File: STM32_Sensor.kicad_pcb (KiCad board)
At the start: 2 copper layers, 35.6 x 20.3 mm, 27 parts, among them J1 Conn Side, J2 Conn Down, J3 Conn Up, J4 Conn Prog, J5 u.FL, SW1 SW_Reset, SW2 SW_BOOT, U1 STM32F103C8Tx, U2 RFM69CW, U3 RFM69HW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

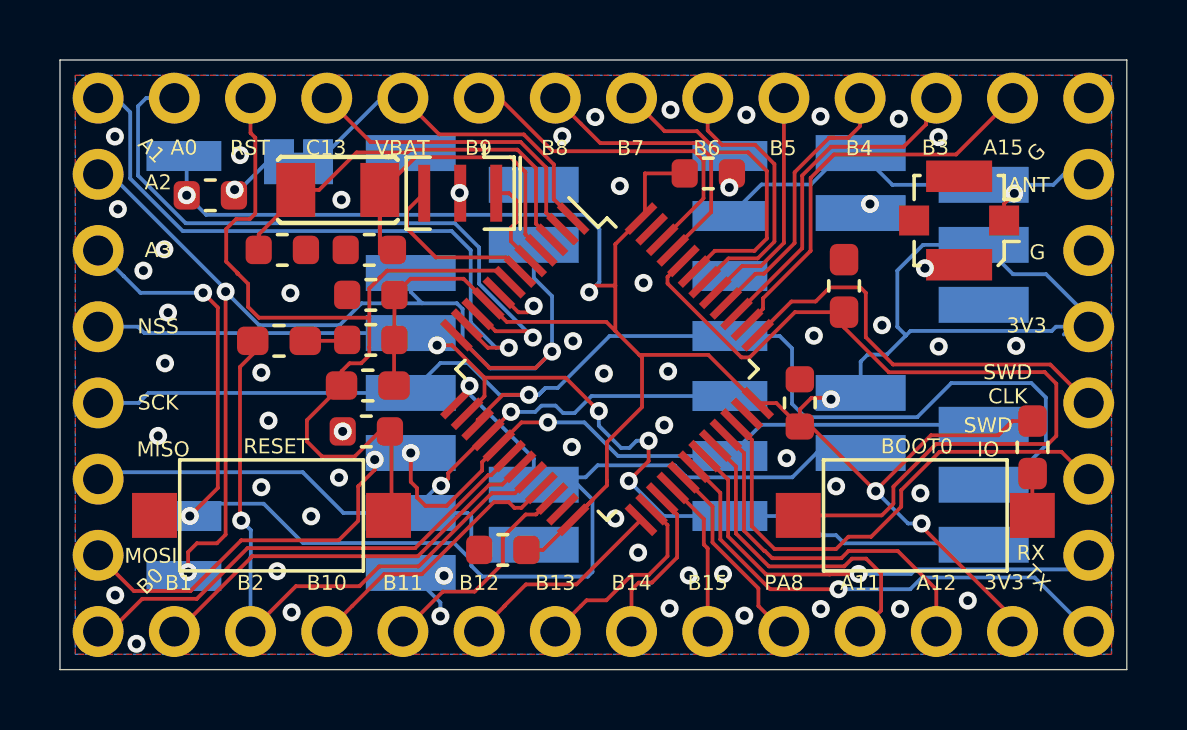
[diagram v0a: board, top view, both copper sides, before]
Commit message: Routed the board with 6 mils traces/clearance
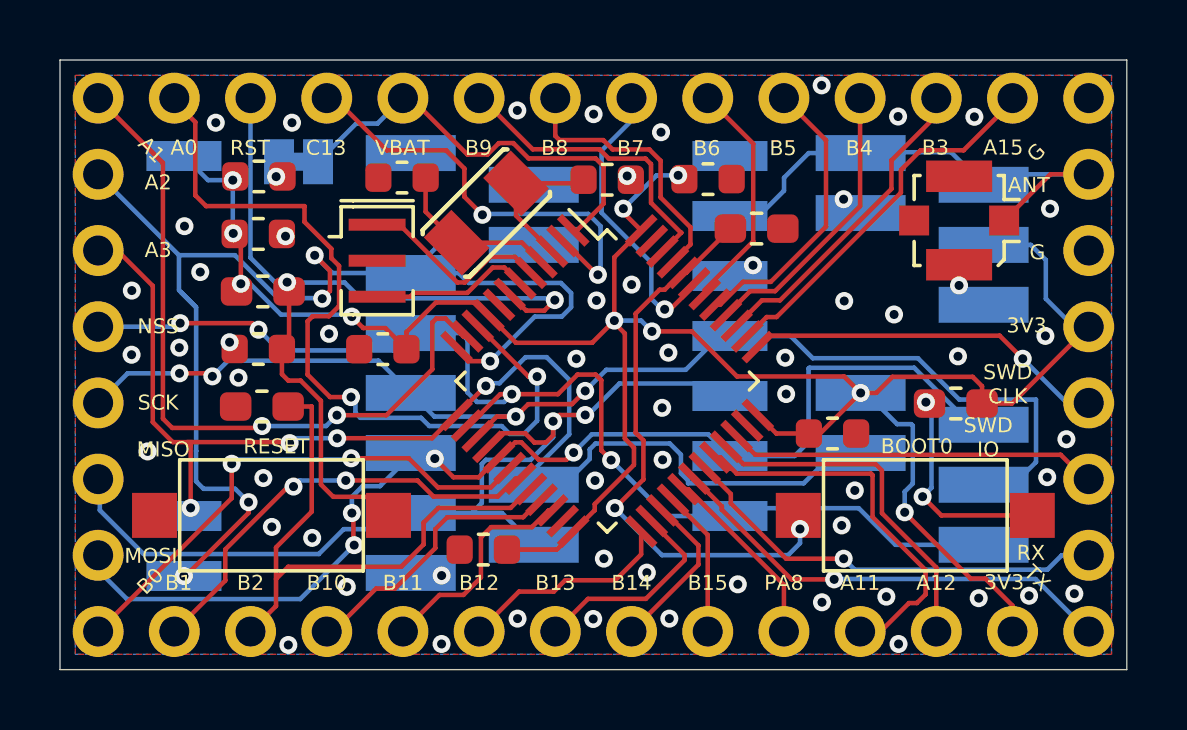
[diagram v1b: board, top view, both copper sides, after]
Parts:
- moved C8 11.1 mm to (145.1, 94.4)
- moved C5 5.15 mm to (133.5, 96.2), turned to 0 degrees
- moved Y1 5.01 mm to (141.1, 95.5), turned to 225 degrees
- moved R1 4.70 mm to (133.7, 98.1), turned to 0 degrees
- moved C1 4.53 mm to (133.5, 100.1)
- moved Y2 3.57 mm to (137.5, 97.1), turned to 270 degrees
- moved R3 3.49 mm to (150.1, 96.0), turned to 180 degrees
- moved R2 2.95 mm to (156.8, 101.9), turned to 180 degrees
- moved C9 2.65 mm to (138.3, 94.3)
- moved R4 2.26 mm to (133.6, 102.0), turned to 0 degrees
- moved C6 1.85 mm to (137.7, 100.1)
- moved C7 1.74 mm to (133.5, 94.3)
- moved C2 1.49 mm to (152.6, 102.9), turned to 0 degrees
- moved C4 0.65 mm to (141.0, 106.7)
- moved U1 0.40 mm to (145.1, 101.1)
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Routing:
- net +3V3: track 94.8 -> 77.4 mm, vias 5 -> 10
- net BOOT0: track 28.6 -> 18.8 mm, vias 0 -> 2
- net RTCOSC1: track 13.9 -> 5.08 mm
- net RTCOSC2: track 12.7 -> 5.69 mm
- net PA3: track 48.3 -> 42.0 mm, vias 3 -> 4
- net GND: track 6.30 -> 0.00 mm, vias 57 -> 59
- net Net-(R2-Pad2): track 1.44 -> 7.26 mm, vias 0 -> 2
- net PA0: track 21.9 -> 27.2 mm, vias 1 -> 2
- net PA2: track 38.6 -> 43.7 mm, vias 3 -> 5
- net SWDIO: track 17.2 -> 12.3 mm
- net PC13: track 10.6 -> 14.6 mm, vias 0 -> 2
- net MOSI: track 35.2 -> 38.7 mm, vias 3 -> 4
- net OSC1: track 3.15 -> 6.49 mm
- net MISO: track 28.7 -> 31.8 mm
- net PA1: track 21.6 -> 24.5 mm, vias 1 -> 2
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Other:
- net class Default: clearance 0.127 -> 0.1524; trace_width 0.127 -> 0.1524
- rule trace_clearance: 0.127 -> 0.1524
- rule trace_min: 0.127 -> 0.1524
